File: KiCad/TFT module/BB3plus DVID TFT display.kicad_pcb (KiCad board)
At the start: 2 copper layers, 136 x 92 mm, 83 parts, among them IC1 TFP401APZP, IC2 AZ1117CH2-3.3TRG1, IC3 TPS61169DCKR, IC4 TCA9554APWR, IC5 TPS2069E, IC6 TSC2007IPWR, IC7 M24C04-RDW6TP, SW1 B3FS-4052P, SW2 B3FS-4052P, SW3 B3FS-4052P, SW4 B3FS-4052P, X1 5051102091, X2 F3311A7H121006E200, X3 F32D-1A7Y1-21040, X4 M22-2010446

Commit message: DVID TFT display BOM update
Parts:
- X1: value 5051102091 -> 505110-2291
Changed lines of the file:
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@@
 			)
 		)
-		(property "Value" "5051102091"
+		(property "Value" "505110-2291"
 			(at 0 0 90)
 			(unlocked yes)
@@
 			)
 		)
-		(attr smd dnp)
+		(attr smd exclude_from_bom dnp)
 		(duplicate_pad_numbers_are_jumpers no)
 		(fp_line
@@
 			)
 		)
-		(property "DigiKey" ""
+		(property "DigiKey" "609-F3311A7H121006E200CT-ND"
 			(at 0 0 180)
 			(unlocked yes)
@@
 			)
 		)
-		(property "Mouser" ""
+		(property "Mouser" "649-311A7H121006E200"
 			(at 0 0 180)
 			(unlocked yes)
@@
 			(keep_text_aligned yes)
 		)
-		(gr_text "1041,3 mils"
+		(gr_text "26,4 mm"
 			(at 113.125 82.39 0)
 			(layer "User.1")
@@
 			(keep_text_aligned yes)
 		)
-		(gr_text "1653,5433 mils"
+		(gr_text "42,0000 mm"
 			(at 122.35 112.4 90)
 			(layer "User.1")
@@
 			(keep_text_aligned yes)
 		)
-		(gr_text "496,1 mils"
+		(gr_text "12,6 mm"
 			(at 92.1 66.3 90)
 			(layer "User.1")
@@
 			(keep_text_aligned yes)
 		)
-		(gr_text "4566,9 mils"
+		(gr_text "116,0 mm"
 			(at 153 143.15 0)
 			(layer "User.1")
@@
 			(keep_text_aligned yes)
 		)
-		(gr_text "3307,1 mils"
+		(gr_text "84,0 mm"
 			(at 223.95 95.5 90)
 			(layer "User.1")
@@
 			(keep_text_aligned yes)
 		)
-		(gr_text "192,9 mils"
+		(gr_text "4,9 mm"
 			(at 208.55 138.05 0)
 			(layer "User.1")
@@
 			(keep_text_aligned yes)
 		)
-		(gr_text "492,1 mils"
+		(gr_text "12,5 mm"
 			(at 93.25 83.15 0)
 			(layer "User.1")
@@
 			(keep_text_aligned yes)
 		)
-		(gr_text "157,5 mils"
+		(gr_text "4,0 mm"
 			(at 223.95 139.5 90)
 			(layer "User.1")
@@
 			(keep_text_aligned yes)
 		)
-		(gr_text "157,5 mils"
+		(gr_text "4,0 mm"
 			(at 223.95 51.500002 90)
 			(layer "User.1")
@@
 			(keep_text_aligned yes)
 		)
-		(gr_text "3622,0 mils"
+		(gr_text "92,0 mm"
 			(at 226.760496 95.5 90)
 			(layer "User.1")
@@
 			(keep_text_aligned yes)
 		)
-		(gr_text "393,7 mils"
+		(gr_text "10,0 mm"
 			(at 90.000001 143.15 0)
 			(layer "User.1")
@@
 			(keep_text_aligned yes)
 		)
-		(gr_text "2653,5 mils"
+		(gr_text "67,4 mm"
 			(at 102.55 93.3 90)
 			(layer "User.1")
@@
 			(keep_text_aligned yes)
 		)
-		(gr_text "622,0472 mils"
+		(gr_text "15,8000 mm"
 			(at 107.8 93.65 0)
 			(layer "User.1")
@@
 			(keep_text_aligned yes)
 		)
-		(gr_text "2983,9 mils"
+		(gr_text "75,8 mm"
 			(at 96.12 95.495 90)
 			(layer "User.1")
@@
 			(keep_text_aligned yes)
 		)
-		(gr_text "393,7 mils"
+		(gr_text "10,0 mm"
 			(at 216 143.15 0)
 			(layer "User.1")
@@
 			(keep_text_aligned yes)
 		)
-		(gr_text "5354,3 mils"
+		(gr_text "136,0 mm"
 			(at 153 145.25 0)
 			(layer "User.1")

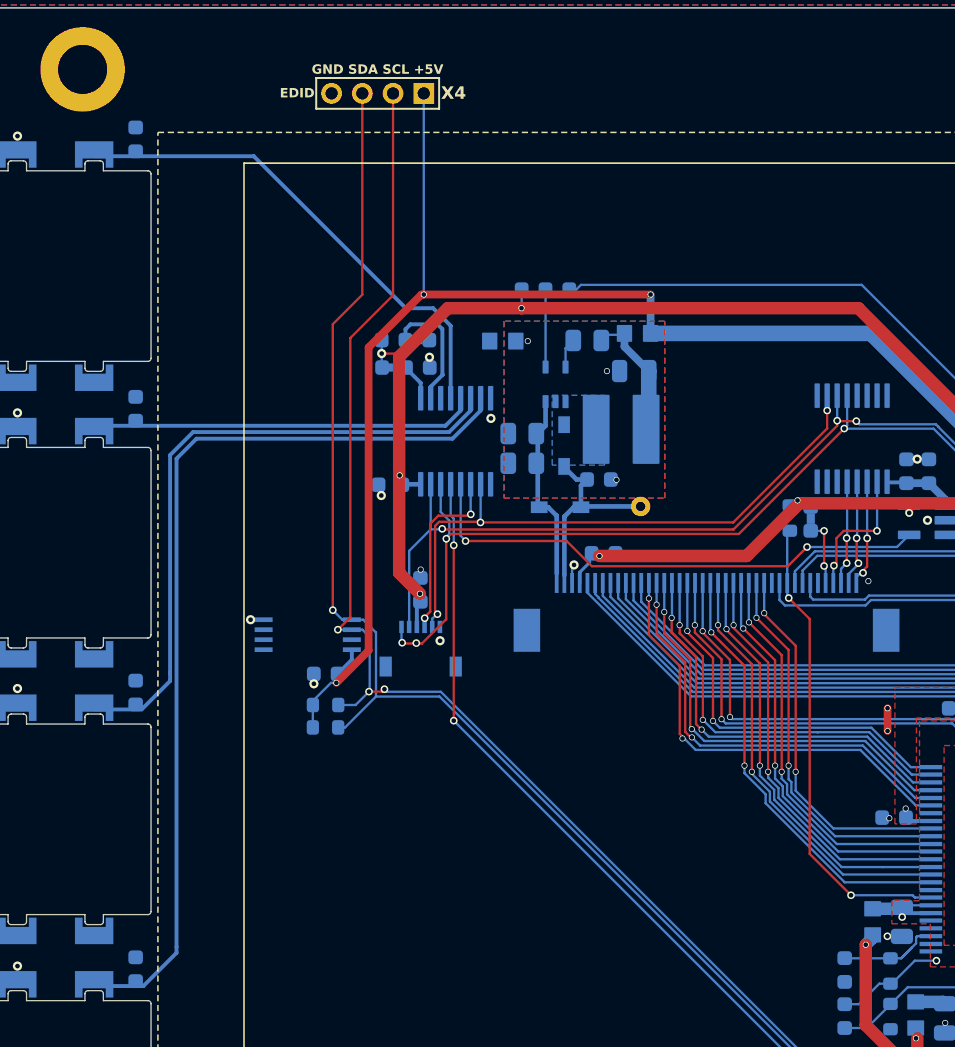
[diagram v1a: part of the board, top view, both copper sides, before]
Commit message: DVID TDFT display JP1 modified
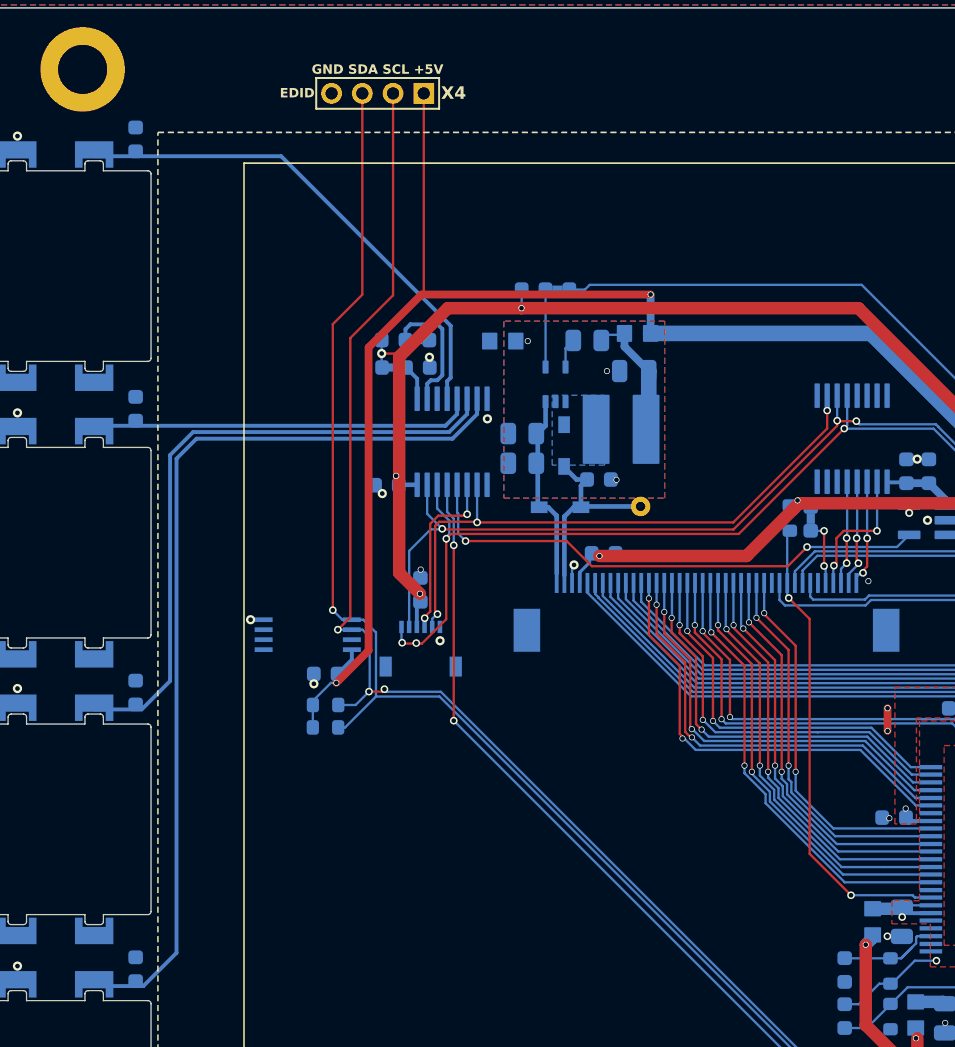
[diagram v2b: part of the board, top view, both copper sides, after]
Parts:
- JP1: footprint PCM_EEZ_SMD:JP3 shorted with 0R (0603) -> PCM_EEZ_SMD:JP3 shorted (0603)
- moved C9 0.23 mm to (114.8, 80.6)
- moved IC4 0.23 mm to (119.1, 77.7)
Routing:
- net +5V: vias 3 -> 2

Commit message: DVID TFT test points positions changed
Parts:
- TP2: moved to F.Cu
- moved TP1 71.2 mm to (127.5, 55.1)
- moved TP3 69.4 mm to (136.8, 55.1)
- moved TP2 26.9 mm to (132.1, 55.1), turned to -90 degrees
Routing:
- net /VLED+: track 13.4 -> 42.4 mm, vias 0 -> 3
- net +5V: track 136.1 -> 144.7 mm

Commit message: Current sense resistor updated
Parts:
- R2: value 10R -> 9R1

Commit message: DVID TFT silkscreen OSHW ID updated
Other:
- board text added: "${project_name} (09/2026 ${project_version})"
- board text added: "HR000122"
- board text removed: "${project_name} (05/2026 ${project_version})"
- board text removed: "HR000121"
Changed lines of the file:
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@@
 		)
 	)
-	(gr_text "${project_name}\n(05/2026 ${project_version})"
+	(gr_text "${project_name}\n(09/2026 ${project_version})"
 		(at 196.1 55.9 0)
 		(layer "B.SilkS")
@@
 		)
 	)
-	(gr_text "HR000121"
+	(gr_text "HR000122"
 		(at 176.067991 56.806597 0)
 		(layer "B.SilkS")
@@
 			(justify left bottom mirror)
 		)
-		(render_cache "HR000121" 0
+		(render_cache "HR000122" 0
 			(polygon
 				(pts
@@
 			(polygon
 				(pts
-					(xy 169.891209 56.514764) (xy 169.67327 56.514764) (xy 169.67327 55.724652) (xy 169.907897 55.776268)
-					(xy 169.907897 55.649214) (xy 169.674697 55.597599) (xy 169.534492 55.597599) (xy 169.534492 56.514764)
-					(xy 169.319345 56.514764) (xy 169.319345 56.633877) (xy 169.891209 56.633877)
+					(xy 169.819741 56.514764) (xy 169.343602 56.514764) (xy 169.343602 56.633877) (xy 169.973098 56.633877)
+					(xy 169.973098 56.514764) (xy 169.746164 56.273562) (xy 169.612225 56.125912) (xy 169.55032 56.043846)
+					(xy 169.518548 55.989057) (xy 169.500231 55.935749) (xy 169.494229 55.881918) (xy 169.500376 55.826323)
+					(xy 169.517576 55.781897) (xy 169.545286 55.746117) (xy 169.582074 55.71949) (xy 169.627837 55.702832)
+					(xy 169.685119 55.696859) (xy 169.748641 55.702317) (xy 169.817694 55.719503) (xy 169.887092 55.747039)
+					(xy 169.964785 55.788179) (xy 169.964785 55.645244) (xy 169.89301 55.615589) (xy 169.82427 55.594807)
+					(xy 169.755148 55.581955) (xy 169.687849 55.577747) (xy 169.612214 55.58331) (xy 169.547366 55.599092)
+					(xy 169.49151 55.624245) (xy 169.443234 55.658644) (xy 169.402719 55.70216) (xy 169.374113 55.751165)
+					(xy 169.356625 55.806771) (xy 169.35055 55.870627) (xy 169.358089 55.936467) (xy 169.381445 56.003946)
+					(xy 169.419538 56.07044) (xy 169.48176 56.151037) (xy 169.594544 56.276043)
 				)
 			)

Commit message: #31
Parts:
- added TP1: PCB_TEST_TABSHIELD, PCM_EEZ_SMD:Testpad 1.6mm, B.Cu at (177.6, 98.6)
- added TP5: PCB_TEST_TABSHIELD, PCM_EEZ_SMD:Testpad 1.6mm, B.Cu at (122.8, 82.0)
- added TP6: PCB_TEST_TABSHIELD, PCM_EEZ_SMD:Testpad 1.6mm, B.Cu at (128.0, 65.8)
- added TP7: PCB_TEST_TABSHIELD, PCM_EEZ_SMD:Testpad 1.6mm, B.Cu at (140.0, 77.4)
- added TP8: PCB_TEST_TABSHIELD, PCM_EEZ_SMD:Testpad 1.6mm, B.Cu at (140.0, 74.8)
- added TP9: PCB_TEST_TABSHIELD, PCM_EEZ_SMD:Testpad 1.6mm, B.Cu at (184.4, 119.9)
- TP2: renamed from TP1; footprint PCM_EEZ_THT:Testhole 24_50mils -> PCM_EEZ_SMD:Testpad 1.6mm
- TP3: renamed from TP2; footprint PCM_EEZ_THT:Testhole 24_50mils -> PCM_EEZ_SMD:Testpad 1.6mm; moved to B.Cu
- TP4: renamed from TP3; footprint PCM_EEZ_THT:Testhole 24_50mils -> PCM_EEZ_SMD:Testpad 1.6mm
- moved TP2 78.9 mm to (184.4, 109.7)
- moved TP4 75.4 mm to (184.4, 113.5)
- moved TP3 27.0 mm to (129.3, 81.9), turned to 90 degrees
- renumbered LOGO6 to LOGO1, LOGO1 to LOGO2, LOGO2 to LOGO3, LOGO3 to LOGO4, LOGO4 to LOGO5, LOGO5 to LOGO6
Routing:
- net /VLED+: track 42.4 -> 11.5 mm, vias 3 -> 0
- net /~{IRQ}: track 97.7 -> 103.4 mm
- net /SCL: track 99.8 -> 104.6 mm
- net /SDA: track 96.9 -> 101.7 mm
- net +3V3: track 230.1 -> 232.7 mm
- net /VLED-: track 12.9 -> 14.8 mm
- net /BL_PWM: track 80.8 -> 82.5 mm
- net +5V: track 144.7 -> 144.0 mm
